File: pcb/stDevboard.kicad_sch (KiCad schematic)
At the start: 21 parts, among them IC1 MPM3610GQV-Z, J1 battery, J11 USB_C_Receptacle_USB2.0_16P, J2 USB_C_Receptacle_USB2.0_16P, J3 Conn_02x03_Top_Bottom

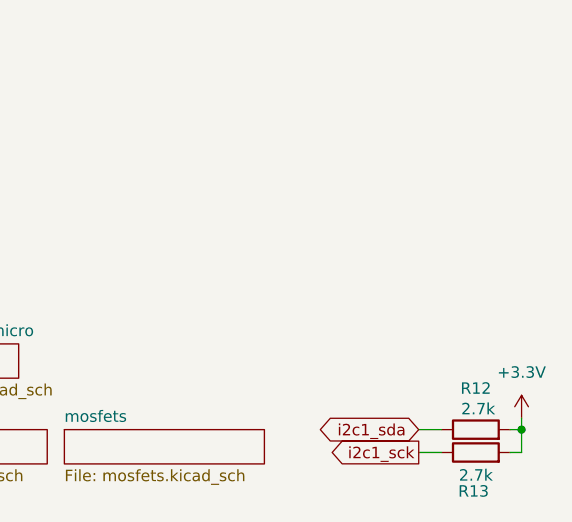
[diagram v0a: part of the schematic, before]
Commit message: board def hopefully done, mpu test firmware written
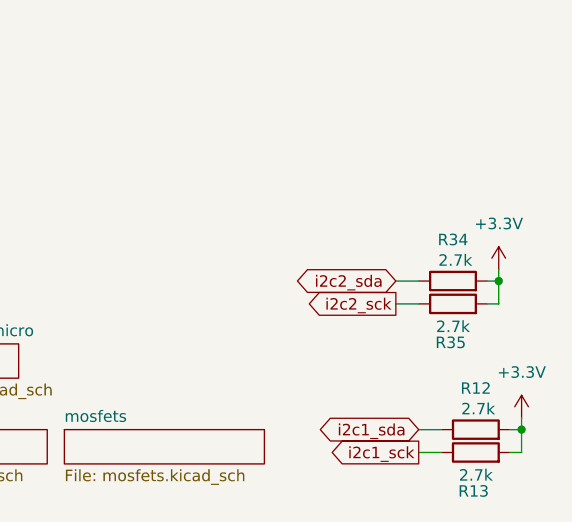
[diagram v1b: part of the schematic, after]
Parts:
- added R34, R35: 2.7k, Resistor_SMD:R_0402_1005Metric, symbol Device:R
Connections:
- net +3.3V: now also R34.2, R35.2
- new net i2c2_sck: R35.1
- new net i2c2_sda: R34.1

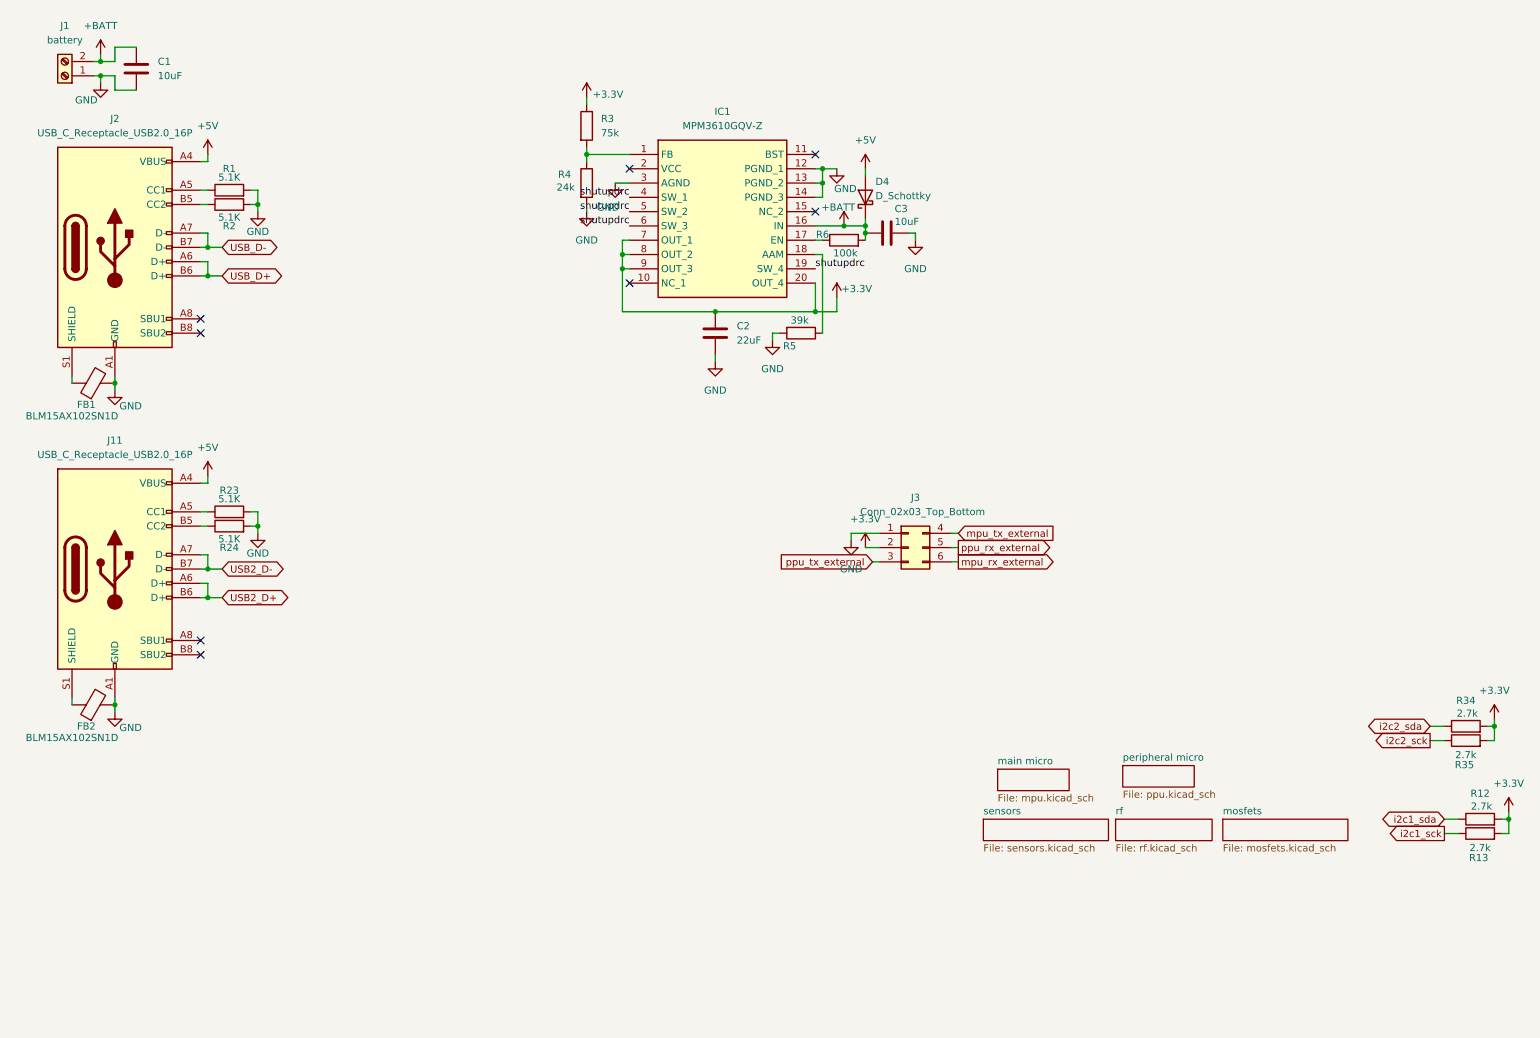
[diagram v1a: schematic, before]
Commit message: added models for some things, fixed micro sd impl and a bunch of other stuff - pcb currently probably ready for production
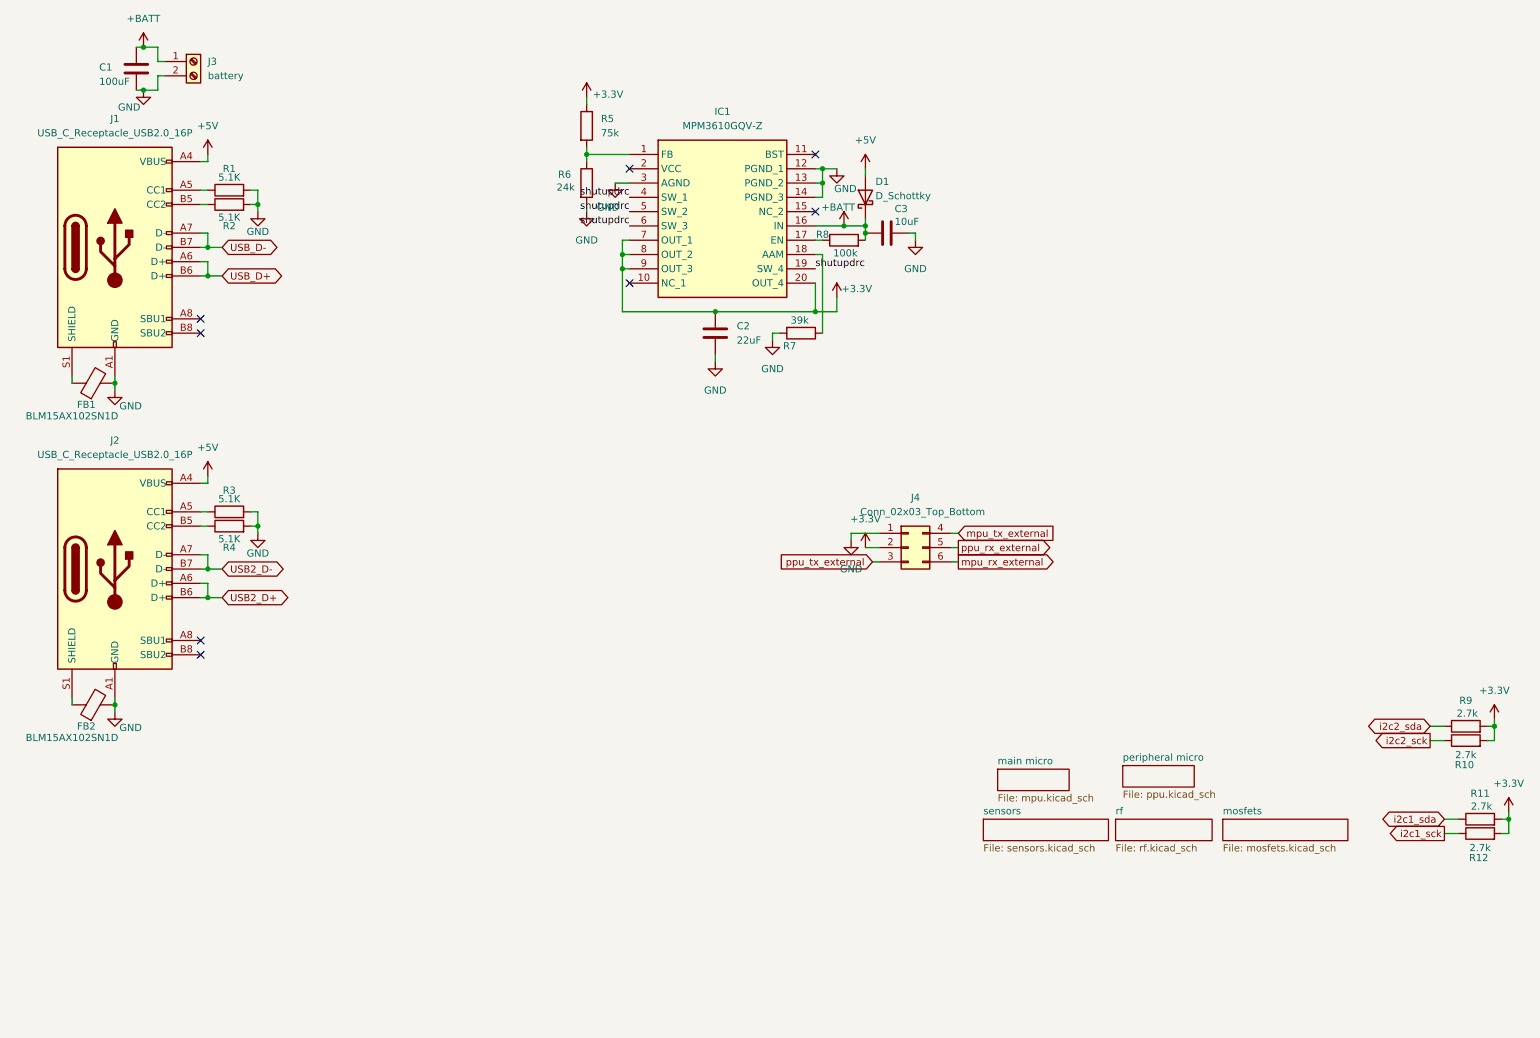
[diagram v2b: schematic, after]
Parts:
- C1: value 10uF -> 100uF
- renumbered D4 to D1, J2 to J1, J11 to J2, J1 to J3, J3 to J4, R35 to R10, R12 to R11, R13 to R12, R23 to R3, R24 to R4, R3 to R5, R4 to R6, R5 to R7, R6 to R8, R34 to R9
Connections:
- net +BATT: now also J3.1 (Pin_1); no longer J3.2 (Pin_2)
- net GND: now also J3.2 (Pin_2); no longer J3.1 (Pin_1)
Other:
- moved on the sheet: J3

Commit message: started making bom - changed some stuff for compatibility with it
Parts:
- C1: value 100uF -> 22uF; footprint Capacitor_SMD:C_0805_2012Metric -> Capacitor_SMD:C_0603_1608Metric
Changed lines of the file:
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@@
 			)
 		)
-		(property "Value" "100uF"
+		(property "Value" "22uF"
 			(at 28.956 26.416 0)
 			(effects
@@
 			)
 		)
-		(property "Footprint" "Capacitor_SMD:C_0805_2012Metric"
+		(property "Footprint" "Capacitor_SMD:C_0603_1608Metric"
 			(at 36.5252 27.94 0)
 			(effects

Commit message: updated pcb from schematic changes, also added some length tuning because why not
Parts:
- renumbered J3 to BAT1
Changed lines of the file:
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@@
 		(dnp no)
 		(fields_autoplaced yes)
-		(property "Reference" "J3"
+		(property "Reference" "BAT1"
 			(at 48.26 22.8599 0)
 			(effects
@@
 			(project ""
 				(path "/d0cafa98-cc2a-4ab3-8dbc-f937bedf434b"
-					(reference "J3")
+					(reference "BAT1")
 					(unit 1)
 				)

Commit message: mainly worked on bom (still just on google sheets), but while doing so fixed some issues and redid some component selection
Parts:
- BAT1: footprint TerminalBlock:TerminalBlock_Xinya_XY308-2.54-2P_1x02_P2.54mm_Horizontal -> footprints:TBC05021GG
- D1: footprint Diode_SMD:D_0805_2012Metric -> Diode_SMD:D_SOD-123
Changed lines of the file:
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@@
 			)
 		)
-		(property "Footprint" "Diode_SMD:D_0805_2012Metric"
+		(property "Footprint" "Diode_SMD:D_SOD-123"
 			(at 165.1 46.99 0)
 			(effects
@@
 			)
 		)
-		(property "Footprint" "TerminalBlock:TerminalBlock_Xinya_XY308-2.54-2P_1x02_P2.54mm_Horizontal"
+		(property "Footprint" "footprints:TBC05021GG"
 			(at 45.72 22.86 0)
 			(effects

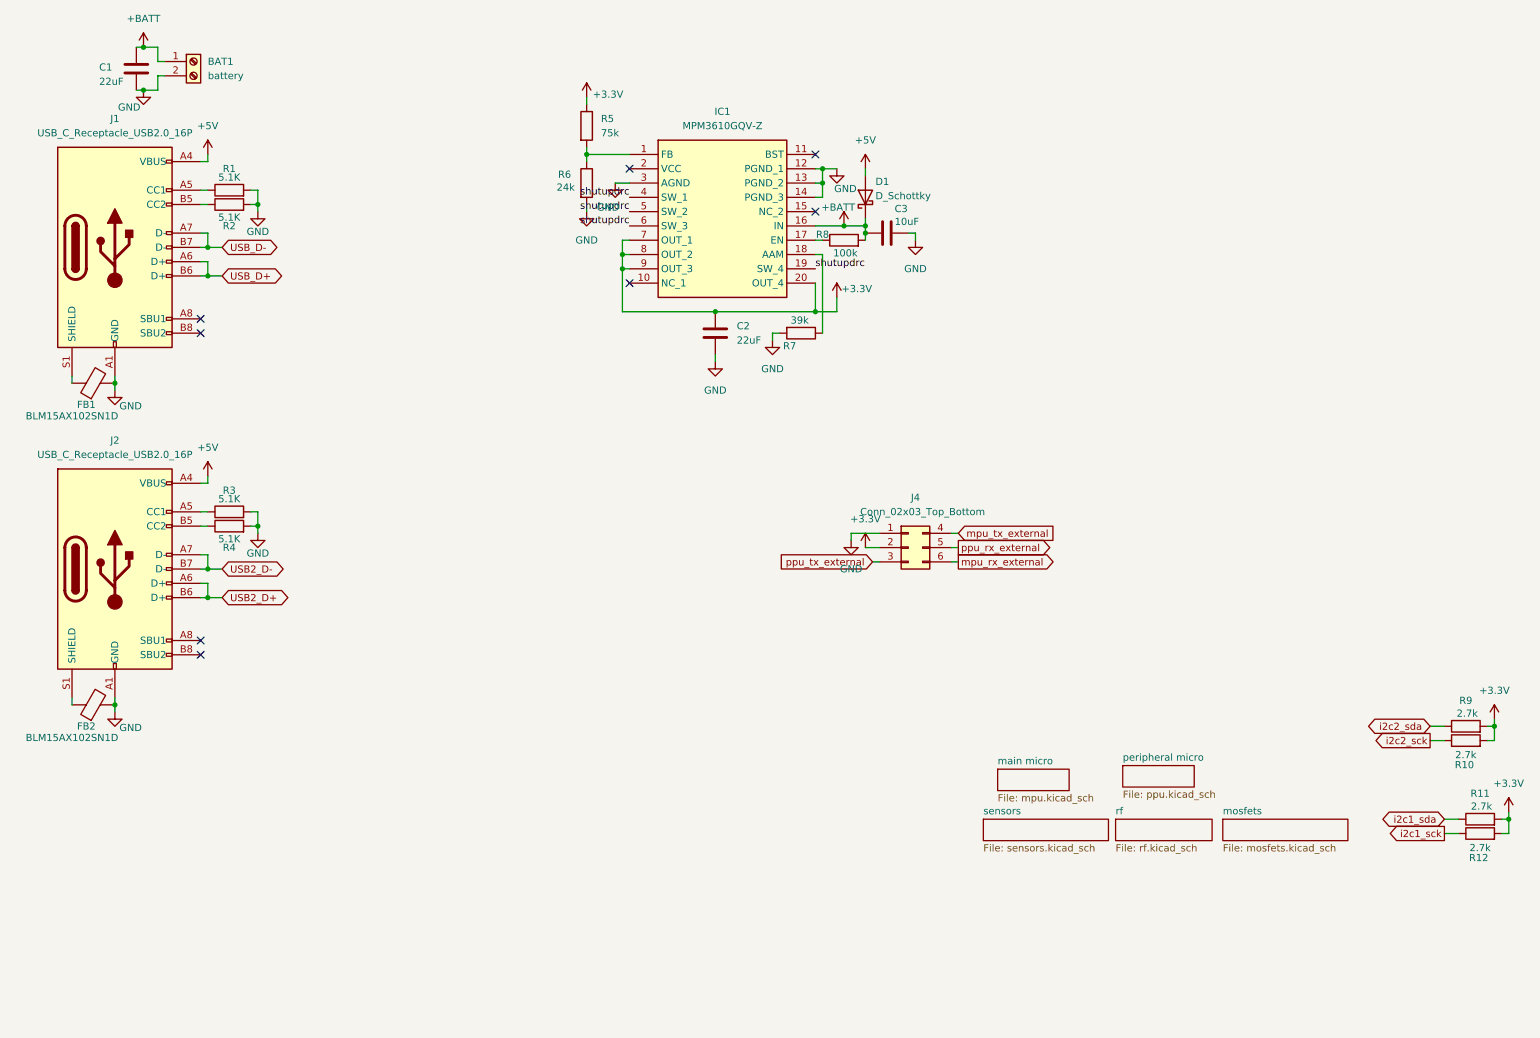
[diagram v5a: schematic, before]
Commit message: reorganized schematic, started to add a readme (not really though), also pcb updated
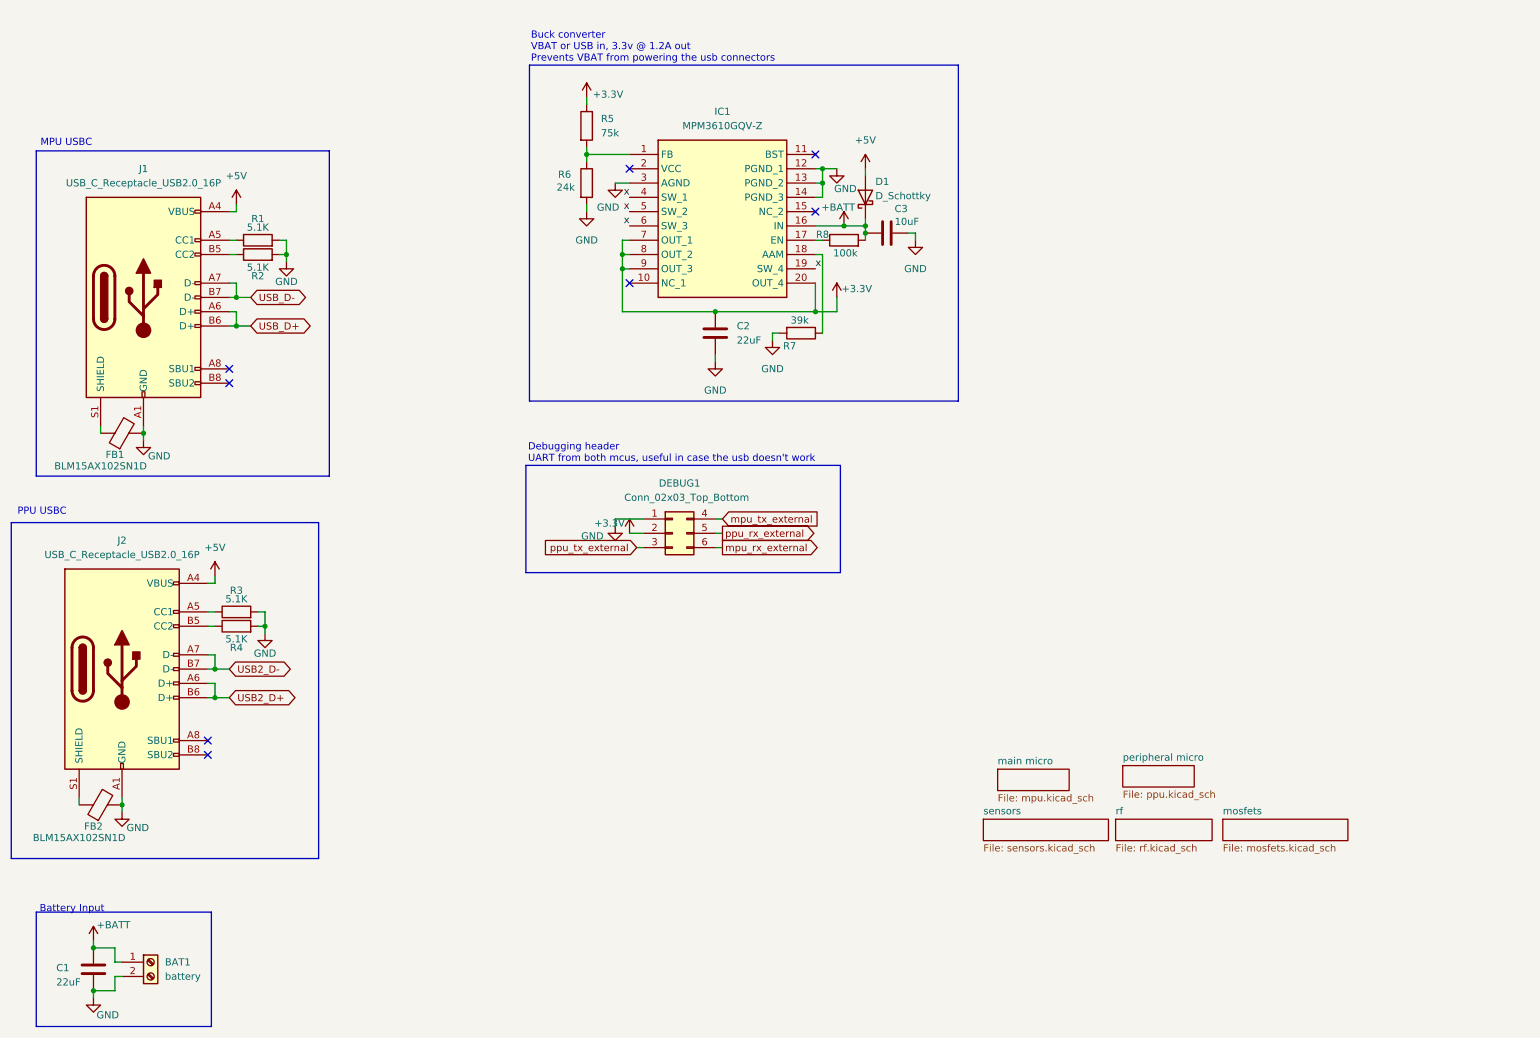
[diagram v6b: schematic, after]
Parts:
- removed R10, R11, R12, R9: 2.7k, Resistor_SMD:R_0402_1005Metric, symbol Device:R
- renumbered J4 to DEBUG1
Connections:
- net shutupdrc renamed x
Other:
- note added: "Battery Input"
- note added: "Buck converter VBAT or USB in, 3.3v @ 1.2A out Prevents VBAT from powering the usb connectors"
- note added: "Debugging header UART from both mcus, useful in case the usb doesn't work"
- note added: "MPU USBC"
- note added: "PPU USBC"
- moved on the sheet: BAT1, C1, DEBUG1, FB1, FB2, J1, J2, R1, R2, R3, R4
